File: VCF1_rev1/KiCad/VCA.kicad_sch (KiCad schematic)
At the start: 17 parts, among them U12 Opamp_Quad, U13 74HC4053, U15 74HC4053, U16 LM13700

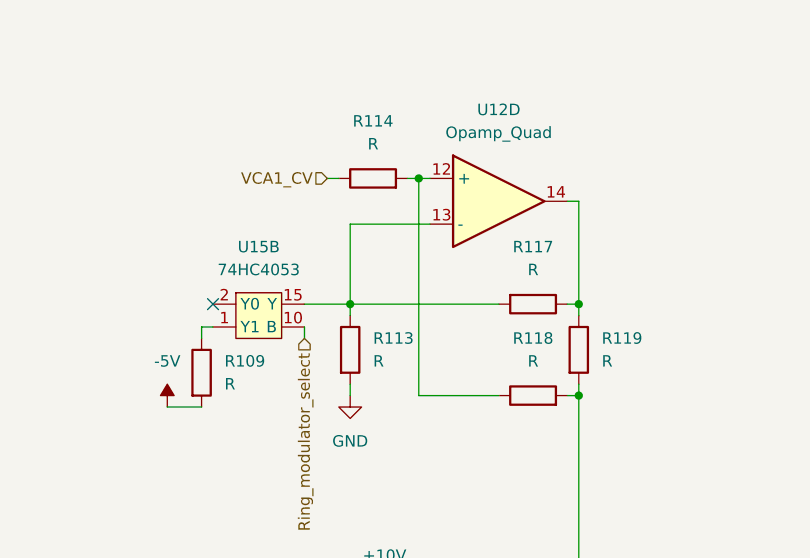
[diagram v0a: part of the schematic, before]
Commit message: Placed more components on the PCB.
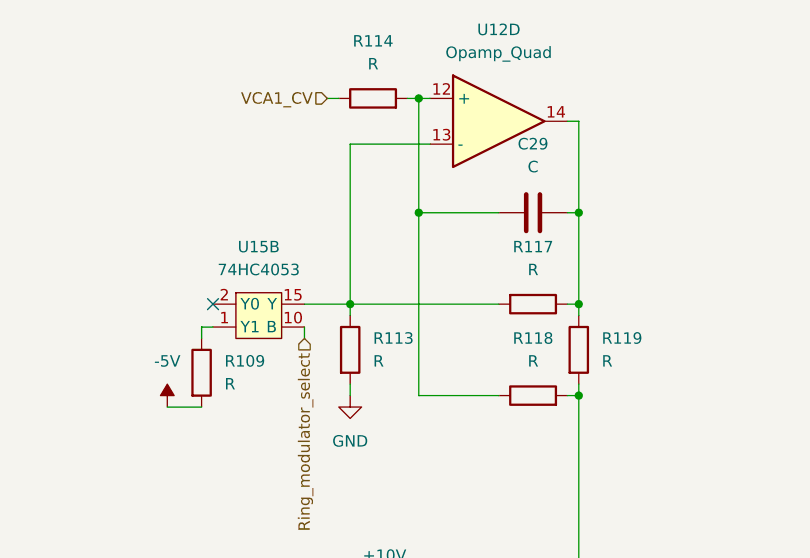
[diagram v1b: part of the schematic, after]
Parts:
- added C29: C, Capacitor_SMD:C_0603_1608Metric, symbol Device:C
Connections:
- net at R117.1, R119.1, U12.14: now also C29.2
- net at R114.2, R118.1, U12.12 (+): now also C29.1
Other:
- moved on the sheet: R114, U12D
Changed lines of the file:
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@@
 (kicad_sch (version 20211123) (generator eeschema)
   (paper "A4")
+  (junction (at 111.76 36.83) (diameter 0) (color 0 0 0 0)
+  )
   (junction (at 134.62 105.41) (diameter 0) (color 0 0 0 0)
   )
@@
   (junction (at 107.95 121.92) (diameter 0) (color 0 0 0 0)
   )
+  (junction (at 129.54 49.53) (diameter 0) (color 0 0 0 0)
+  )
   (junction (at 77.47 114.3) (diameter 0) (color 0 0 0 0)
   )
   (junction (at 151.13 107.95) (diameter 0) (color 0 0 0 0)
   )
+  (junction (at 111.76 49.53) (diameter 0) (color 0 0 0 0)
+  )
   (junction (at 129.54 59.69) (diameter 0) (color 0 0 0 0)
   )
@@
   )
   (junction (at 77.47 102.87) (diameter 0) (color 0 0 0 0)
-  )
-  (junction (at 111.76 45.72) (diameter 0) (color 0 0 0 0)
   )
   (junction (at 99.06 111.76) (diameter 0) (color 0 0 0 0)
@@
   (no_connect (at 88.9 59.69))
   (no_connect (at 78.74 111.76))
-  (wire (pts (xy 104.14 50.8) (xy 104.14 59.69))
-    (stroke (width 0) (type default) (color 0 0 0 0))
-  )
-  (wire (pts (xy 104.14 50.8) (xy 113.03 50.8))
+  (wire (pts (xy 104.14 41.91) (xy 104.14 59.69))
+    (stroke (width 0) (type default) (color 0 0 0 0))
+  )
+  (wire (pts (xy 104.14 41.91) (xy 113.03 41.91))
     (stroke (width 0) (type default) (color 0 0 0 0))
   )
@@
     (stroke (width 0) (type default) (color 0 0 0 0))
   )
+  (wire (pts (xy 129.54 49.53) (xy 129.54 59.69))
+    (stroke (width 0) (type default) (color 0 0 0 0))
+  )
   (wire (pts (xy 107.95 105.41) (xy 115.57 105.41))
     (stroke (width 0) (type default) (color 0 0 0 0))
@@
     (stroke (width 0) (type default) (color 0 0 0 0))
   )
-  (wire (pts (xy 111.76 45.72) (xy 113.03 45.72))
-    (stroke (width 0) (type default) (color 0 0 0 0))
-  )
-  (wire (pts (xy 111.76 69.85) (xy 111.76 45.72))
+  (wire (pts (xy 111.76 49.53) (xy 120.65 49.53))
+    (stroke (width 0) (type default) (color 0 0 0 0))
+  )
+  (wire (pts (xy 111.76 49.53) (xy 111.76 69.85))
+    (stroke (width 0) (type default) (color 0 0 0 0))
+  )
+  (wire (pts (xy 111.76 36.83) (xy 113.03 36.83))
+    (stroke (width 0) (type default) (color 0 0 0 0))
+  )
+  (wire (pts (xy 111.76 36.83) (xy 111.76 49.53))
     (stroke (width 0) (type default) (color 0 0 0 0))
   )
@@
     (stroke (width 0) (type default) (color 0 0 0 0))
   )
-  (wire (pts (xy 128.27 48.26) (xy 129.54 48.26))
-    (stroke (width 0) (type default) (color 0 0 0 0))
-  )
-  (wire (pts (xy 129.54 48.26) (xy 129.54 59.69))
+  (wire (pts (xy 128.27 39.37) (xy 129.54 39.37))
+    (stroke (width 0) (type default) (color 0 0 0 0))
+  )
+  (wire (pts (xy 129.54 39.37) (xy 129.54 49.53))
     (stroke (width 0) (type default) (color 0 0 0 0))
   )
@@
     (stroke (width 0) (type default) (color 0 0 0 0))
   )
-  (wire (pts (xy 101.6 45.72) (xy 102.87 45.72))
+  (wire (pts (xy 101.6 36.83) (xy 102.87 36.83))
     (stroke (width 0) (type default) (color 0 0 0 0))
   )
@@
     (stroke (width 0) (type default) (color 0 0 0 0))
   )
-  (wire (pts (xy 110.49 45.72) (xy 111.76 45.72))
+  (wire (pts (xy 110.49 36.83) (xy 111.76 36.83))
     (stroke (width 0) (type default) (color 0 0 0 0))
   )
@@
   )
   (wire (pts (xy 88.9 111.76) (xy 90.17 111.76))
+    (stroke (width 0) (type default) (color 0 0 0 0))
+  )
+  (wire (pts (xy 128.27 49.53) (xy 129.54 49.53))
     (stroke (width 0) (type default) (color 0 0 0 0))
   )
@@
     (effects (font (size 1.27 1.27)) (justify right))
   )
-  (hierarchical_label "VCA1_CV" (shape input) (at 101.6 45.72 180)
+  (hierarchical_label "VCA1_CV" (shape input) (at 101.6 36.83 180)
     (effects (font (size 1.27 1.27)) (justify right))
   )
@@
     (pin "9")
   )
-  (symbol (lib_id "Device:Opamp_Quad") (at 120.65 48.26 0) (unit 4)
-    (in_bom yes) (on_board yes) (fields_autoplaced)
-    (property "Reference" "U12" (id 0) (at 120.65 38.1 0))
-    (property "Value" "Opamp_Quad" (id 1) (at 120.65 40.64 0))
-    (property "Footprint" "Package_SO:SOIC-14_3.9x8.7mm_P1.27mm" (id 2) (at 120.65 48.26 0)
-      (effects (font (size 1.27 1.27)) hide)
-    )
-    (property "Datasheet" "~" (id 3) (at 120.65 48.26 0)
+  (symbol (lib_id "Device:Opamp_Quad") (at 120.65 39.37 0) (unit 4)
+    (in_bom yes) (on_board yes) (fields_autoplaced)
+    (property "Reference" "U12" (id 0) (at 120.65 29.21 0))
+    (property "Value" "Opamp_Quad" (id 1) (at 120.65 31.75 0))
+    (property "Footprint" "Package_SO:SOIC-14_3.9x8.7mm_P1.27mm" (id 2) (at 120.65 39.37 0)
+      (effects (font (size 1.27 1.27)) hide)
+    )
+    (property "Datasheet" "~" (id 3) (at 120.65 39.37 0)
       (effects (font (size 1.27 1.27)) hide)
     )
@@
     )
     (property "Datasheet" "~" (id 3) (at 93.98 102.87 0)
+      (effects (font (size 1.27 1.27)) hide)
+    )
+    (pin "1")
+    (pin "2")
+  )
+  (symbol (lib_id "Device:C") (at 124.46 49.53 90) (unit 1)
+    (in_bom yes) (on_board yes) (fields_autoplaced)
+    (property "Reference" "C29" (id 0) (at 124.46 41.91 90))
+    (property "Value" "C" (id 1) (at 124.46 44.45 90))
+    (property "Footprint" "Capacitor_SMD:C_0603_1608Metric" (id 2) (at 128.27 48.5648 0)
+      (effects (font (size 1.27 1.27)) hide)
+    )
+    (property "Datasheet" "~" (id 3) (at 124.46 49.53 0)
       (effects (font (size 1.27 1.27)) hide)
     )
@@
     (pin "16")
   )
-  (symbol (lib_id "Device:R") (at 106.68 45.72 90) (unit 1)
-    (in_bom yes) (on_board yes) (fields_autoplaced)
-    (property "Reference" "R114" (id 0) (at 106.68 39.37 90))
-    (property "Value" "R" (id 1) (at 106.68 41.91 90))
-    (property "Footprint" "Resistor_SMD:R_0603_1608Metric" (id 2) (at 106.68 47.498 90)
-      (effects (font (size 1.27 1.27)) hide)
-    )
-    (property "Datasheet" "~" (id 3) (at 106.68 45.72 0)
-      (effects (font (size 1.27 1.27)) hide)
-    )
+  (symbol (lib_id "Device:R") (at 106.68 36.83 90) (unit 1)
+    (in_bom yes) (on_board yes) (fields_autoplaced)
+    (property "Reference" "R114" (id 0) (at 106.68 30.48 90))
+    (property "Value" "R" (id 1) (at 106.68 33.02 90))
+    (property "Footprint" "Resistor_SMD:R_0603_1608Metric" (id 2) (at 106.68 38.608 90)
+      (effects (font (size 1.27 1.27)) hide)
+    )
+    (property "Datasheet" "~" (id 3) (at 106.68 36.83 0)
+      (effects (font (size 1.27 1.27)) hide)
+    )
